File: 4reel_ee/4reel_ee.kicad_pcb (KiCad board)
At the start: 4 copper layers, 117.5 x 30 mm, 152 parts, among them J1 USB_C_Receptacle_USB2.0_16P, J2 Micro_SD_Card_Det2, J3 RJ45_Hanrun_HR911105A_Horizon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, J4 JST, U1 RV1103G, U2 EA3036C, U3 ImageSensor_OV9281, U4 TLV73312PDBV, U5 TPD2EUSB30, U6 TLV73328PDBV, U7 W25Q32JVZP, U8 LIS2HH12, U9 ImageSensor_OV9281, Y1 TXC-7C, Y2 24Mhz, Y3 TXC-7C

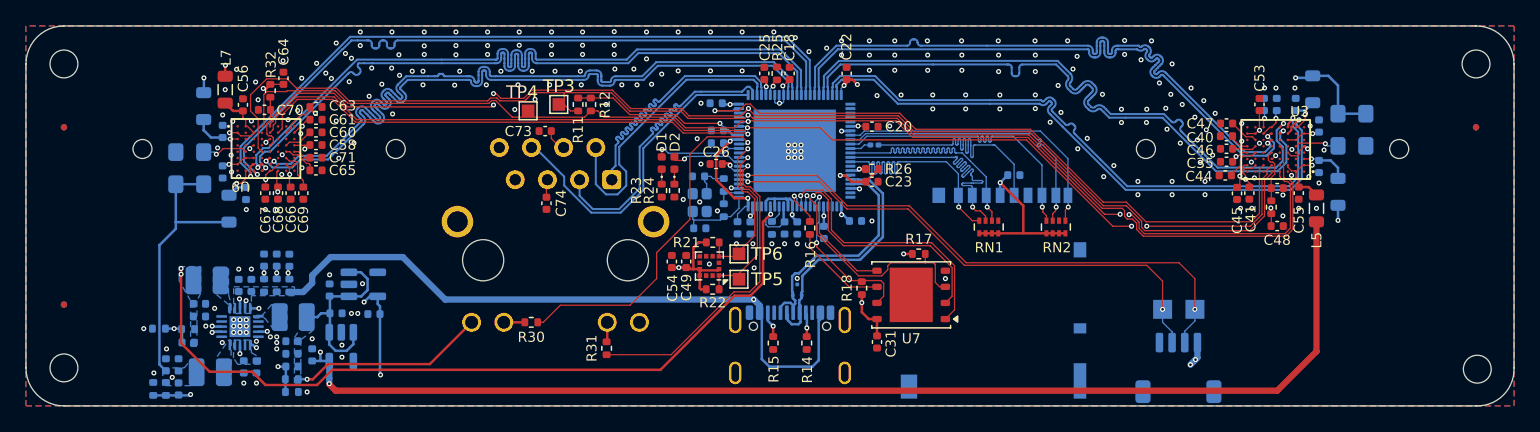
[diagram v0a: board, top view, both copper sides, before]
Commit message: Initial schematic, routing finished for RV1106 based design.
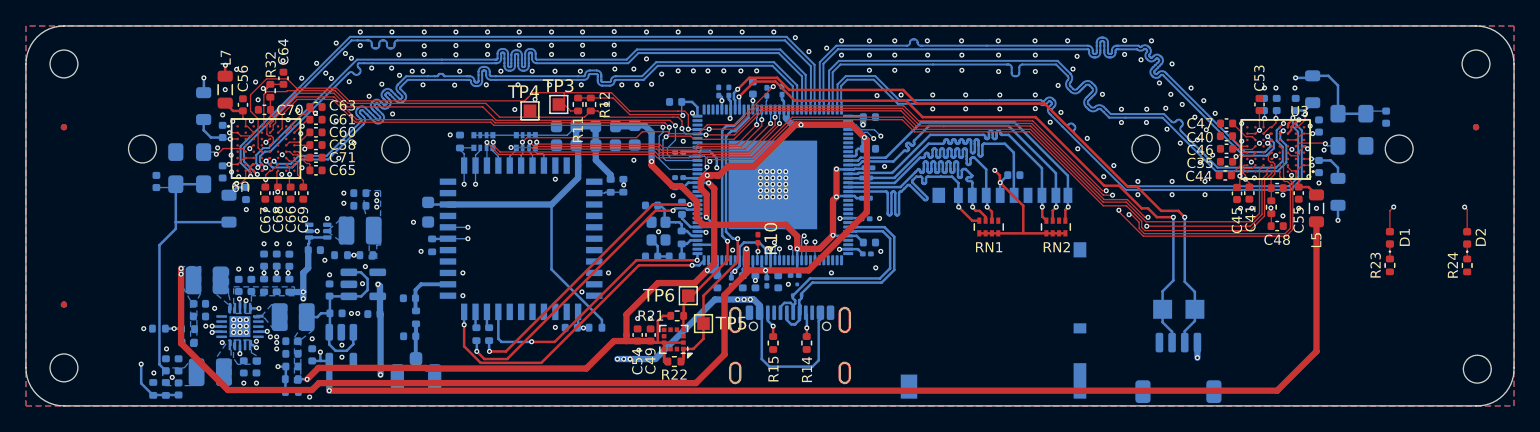
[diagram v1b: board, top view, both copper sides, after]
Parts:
- removed R18, R26: 10k, Resistor_SMD:R_0402_1005Metric
- added C76: 100nF, Capacitor_SMD:C_0201_0603Metric, B.Cu at (123.7, 105.2)
- added C77: 10uF, Capacitor_SMD:C_0402_1005Metric, B.Cu at (127.4, 105.2)
- added C78: 100nF, Capacitor_SMD:C_0201_0603Metric, B.Cu at (134.3, 100.2)
- added C79: 10uF, Capacitor_SMD:C_0402_1005Metric, B.Cu at (94.4, 99.2)
- added C80: 100nF, Capacitor_SMD:C_0201_0603Metric, B.Cu at (134.3, 98.6)
- added C81: 10uF, Capacitor_SMD:C_0603_1608Metric, B.Cu at (110.7, 94.4)
- added C82: NC, Capacitor_SMD:C_0402_1005Metric, B.Cu at (111.1, 108.8)
- added C83: 10uF, Capacitor_SMD:C_0603_1608Metric, B.Cu at (110.7, 92.9)
- added C84: 10uF, Capacitor_SMD:C_0603_1608Metric, B.Cu at (116.1, 93.6)
- added C85: 10uF, Capacitor_SMD:C_0603_1608Metric, B.Cu at (113.8, 94.4)
- added C86: 100nF, Capacitor_SMD:C_0201_0603Metric, B.Cu at (119.6, 95.0)
- added C87: 100nF, Capacitor_SMD:C_0201_0603Metric, B.Cu at (119.6, 97.0)
- added C88: 100nF, Capacitor_SMD:C_0201_0603Metric, B.Cu at (119.6, 97.8)
- added C89: 100nF, Capacitor_SMD:C_0201_0603Metric, B.Cu at (123.5, 90.2)
- added C90: 100nF, Capacitor_SMD:C_0201_0603Metric, B.Cu at (134.5, 96.2)
- added C91: 100nF, Capacitor_SMD:C_0201_0603Metric, B.Cu at (122.7, 90.2)
- added C92: 10uF, Capacitor_SMD:C_0603_1608Metric, B.Cu at (99.8, 99.7)
- added C93: 10uF, Capacitor_SMD:C_0402_1005Metric, B.Cu at (94.4, 98.2)
- added L10: 120R@100MHz, Inductor_SMD:L_0603_1608Metric, B.Cu at (113.8, 92.9)
- added L11: 1uH, Inductor_SMD:L_1008_2520Metric, B.Cu at (94.4, 101.2)
- added R28: 22R, Resistor_SMD:R_0201_0603Metric, B.Cu at (126.5, 90.2)
- added R29: 1k, Resistor_SMD:R_0402_1005Metric, B.Cu at (104.6, 109.3)
- added R33: 1k, Resistor_SMD:R_0402_1005Metric, B.Cu at (103.6, 109.3)
- added R34: 100k, Resistor_SMD:R_0402_1005Metric, B.Cu at (113.0, 108.8)
- added R35: 10k, Resistor_SMD:R_0402_1005Metric, B.Cu at (114.2, 97.6)
- added R36: 0R, Resistor_SMD:R_0402_1005Metric, B.Cu at (115.2, 97.6)
- added RN3: 10k, Resistor_SMD:R_Array_Convex_4x0402, B.Cu at (104.1, 94.1)
- added RN4: 10k, Resistor_SMD:R_Array_Convex_4x0402, B.Cu at (107.5, 94.1)
- added U10: RTL8723DS, KiLib:RTL8723, B.Cu at (107.1, 101.8)
- C18: footprint Capacitor_SMD:C_0402_1005Metric -> Capacitor_SMD:C_0201_0603Metric; moved to B.Cu
- C20, C22, C23, C25, C26: moved to B.Cu
- C24, C28, C75: footprint Capacitor_SMD:C_0402_1005Metric -> Capacitor_SMD:C_0201_0603Metric
- C31: value 100nF -> 10uF; moved to B.Cu
- C73, C74: value 10nF -> NC; moved to B.Cu
- J3: value RJ45_Hanrun_HR911105A_Horizontal -> Conn_Coaxial; footprint Connector_RJ:RJ45_Hanrun_HR911105A_Horizontal -> Connector_Coaxial:U.FL_Hirose_U.FL-R-SMT-1_Vertical
- R10: footprint Resistor_SMD:R_0402_1005Metric -> Resistor_SMD:R_0201_0603Metric; moved to F.Cu
- R16: value 22R -> 100k; moved to B.Cu
- R17: value 10k -> 80k; moved to B.Cu
- R25: value 6.04k -> 10K; moved to B.Cu
- R30: value 330R -> 0R; moved to B.Cu
- R31: value 330R -> 100K; moved to B.Cu
- U1: value RV1103G -> RV1106G3; footprint rv1103b:Rockchip_QFN-88-1EP_9x9mm_P0.35mm_EP6.5x6.5mm -> rv1106:Rockchip_QFN-128-1EP_12.3x12.3mm_P0.35mm_EP7x7mm
- U7: value W25Q32JVZP -> TPS62A01ADRL; footprint Package_SON:WSON-8-1EP_6x5mm_P1.27mm_EP3.4x4.3mm -> Package_TO_SOT_SMD:SOT-563; moved to B.Cu
- moved D2 62.9 mm to (181.8, 101.7)
- moved R24 62.9 mm to (181.8, 103.9)
- moved D1 57.8 mm to (175.7, 101.7)
- moved R23 57.8 mm to (175.7, 103.9)
- moved C37 52.8 mm to (175.4, 92.2), turned to -90 degrees
- moved U7 47.1 mm to (91.1, 101.2)
- moved R17 45.6 mm to (92.9, 103.1), turned to 180 degrees
- moved C31 45.0 mm to (90.8, 102.7), turned to 0 degrees
- moved C72 44.6 mm to (78.3, 97.3), turned to 90 degrees
- moved R16 35.1 mm to (94.9, 103.1), turned to 180 degrees
- moved R25 25.6 mm to (102.3, 94.1)
- moved J3 22.0 mm to (98.8, 112.8), turned to -90 degrees
- moved C73 19.4 mm to (98.3, 109.5)
- moved R31 16.0 mm to (100.1, 102.3)
- moved C22 13.7 mm to (119.3, 91.0), turned to 180 degrees
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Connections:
- net /MPU/SDMMC.CLK renamed /MPU/SDMMC1.CLK
- C31 pad 1: +3V3 -> +5V
- C32 pad 1: Net-(U1GPIO / Peripherals-OSC_SOC_XIN) -> Net-(U1Analog / Connectivity-OSC_XOUT)
- C73 pad 1: Net-(J3-TCT) -> Net-(J3-In)
- C74 pad 1: Net-(J3-RCT) -> Net-(U10-WIFI/BT_ANT)
- J2 pad 1: /MPU/SDMMC.D2 -> /MPU/SDMMC1.D2
- J2 pad 2: /MPU/SDMMC.D3 -> /MPU/SDMMC1.D3
- J2 pad 3: /MPU/SDMMC.CMD -> /MPU/SDMMC1.CMD
- J2 pad 7: /MPU/SDMMC.D0 -> /MPU/SDMMC1.D0
- J2 pad 8: /MPU/SDMMC.D1 -> /MPU/SDMMC1.D1
- J2 pad 9: /MPU/SDMMC.DET -> /MPU/SDMMC1.DET
- J3 pad 1: /MPU/EPHY.TXP -> Net-(J3-In)
- J3 pad 2: /MPU/EPHY.TXN -> GND
- R10 pad 2: Net-(U1Analog / High-Speed-DRAM_ZQ) -> Net-(U1Analog / Connectivity-DRAM_ZQ)
- R16 pad 1: Net-(U1Analog / High-Speed-FSPI_CLK) -> +1V35
- R16 pad 2: /Flash/FSPI.CLK -> Net-(U7-FB)
- R17 pad 1: +3V3 -> Net-(U7-FB)
- R17 pad 2: /Flash/FSPI.D2 -> GND
- R19 pad 2: Net-(U1GPIO / Peripherals-OSC_SOC_XOUT) -> Net-(U1Analog / Connectivity-OSC_XIN)
- R20 pad 1: Net-(U1GPIO / Peripherals-OSC_SOC_XOUT) -> Net-(U1Analog / Connectivity-OSC_XIN)
- R20 pad 2: Net-(U1GPIO / Peripherals-OSC_SOC_XIN) -> Net-(U1Analog / Connectivity-OSC_XOUT)
- R25 pad 2: Net-(U1Analog / High-Speed-FEPHY_EXTR) -> /MPU/WL_REG_ON
- R27 pad 1: Net-(U1GPIO / Peripherals-SDMMC_CLK) -> Net-(U1Storage-SDMMC0_CLK)
- R30 pad 1: /LED_ACT -> Net-(J3-In)
- R30 pad 2: Net-(J3-Pad11) -> Net-(U10-WIFI/BT_ANT)
- R31 pad 1: /LED100 -> GND
- R31 pad 2: Net-(J3-Pad10) -> /MPU/BT_WAKE
- RN1 pad 2: /MPU/SDMMC.CMD -> /MPU/SDMMC1.CMD
- RN1 pad 3: /MPU/SDMMC.D3 -> /MPU/SDMMC1.D3
- RN1 pad 4: /MPU/SDMMC.D2 -> /MPU/SDMMC1.D2
- RN2 pad 1: /MPU/SDMMC.DET -> /MPU/SDMMC1.DET
- RN2 pad 3: /MPU/SDMMC.D1 -> /MPU/SDMMC1.D1
- RN2 pad 4: /MPU/SDMMC.D0 -> /MPU/SDMMC1.D0
- U1 pad 1: unconnected-(U1Analog / High-Speed-MIPI_CLK0_OUT-Pad1) -> +1V8
- U1 pad 10: /MPU/SDMMC.D0 -> +0V9
- U1 pad 11: Net-(U1GPIO / Peripherals-SDMMC_CLK) -> /MPU/SDMMC1.DET
- U1 pad 12: /MPU/SDMMC.CMD -> /MPU/SDMMC1.D1
- U1 pad 13: /MPU/SDMMC.D3 -> +3V3
- U1 pad 14: /MPU/SDMMC.D2 -> /MPU/SDMMC1.D0
- U1 pad 15: unconnected-(U1Analog / High-Speed-SARADC_IN1-Pad15) -> Net-(U1Storage-SDMMC0_CLK)
- U1 pad 16: Net-(U1Analog / High-Speed-SARADC_IN0) -> /MPU/SDMMC1.CMD
- U1 pad 17: +1V8 -> /MPU/SDMMC1.D3
- U1 pad 18: /MPU/USB.DN -> /MPU/SDMMC1.D2
- U1 pad 19: /MPU/USB.DP -> +3V3
- U1 pad 20: +3V3 -> unconnected-(U1Analog / Connectivity-RTC_XOUT-Pad20)
- U1 pad 23: +1V8 -> unconnected-(U1Analog / Connectivity-SARADC_IN0-Pad23)
- U1 pad 24: unconnected-(U1GPIO / Peripherals-CODEC_MIC0P_MICP-Pad24) -> +1V8
- U1 pad 26: unconnected-(U1GPIO / Peripherals-CODEC_MIC1P_MICN-Pad26) -> /MPU/USB.DN
- U1 pad 27: +3V3 -> /MPU/USB.DP
- U1 pad 28: /Flash/FSPI.D3 -> +3V3
- U1 pad 29: /Flash/FSPI.D0 -> unconnected-(U1Analog / Connectivity-CODEC_LINEOUT-Pad29)
- U1 pad 3: unconnected-(U1GPIO / Peripherals-PWM7_IR_M2-Pad3) -> /MPU/LED2
- U1 pad 30: /Flash/FSPI.D1 -> unconnected-(U1Analog / Connectivity-CODEC_VCM-Pad30)
- U1 pad 31: /Flash/FSPI.D2 -> +1V8
- U1 pad 32: /Flash/FSPI.~{CS} -> unconnected-(U1Analog / Connectivity-CODEC_MICBIAS-Pad32)
- U1 pad 33: Net-(U1Analog / High-Speed-FSPI_CLK) -> unconnected-(U1Analog / Connectivity-CODEC_MIC0N-Pad33)
- U1 pad 34: +1V8 -> unconnected-(U1Analog / Connectivity-CODEC_MIC0P-Pad34)
- U1 pad 35: +1V8 -> unconnected-(U1Analog / Connectivity-CODEC_MIC1N-Pad35)
- U1 pad 36: +0V9 -> unconnected-(U1Analog / Connectivity-CODEC_MIC1P-Pad36)
- U1 pad 37: Net-(U1Analog / High-Speed-DRAM_ZQ) -> GND
- U1 pad 38: +1V8 -> unconnected-(U1Storage-EMMC_D5-Pad38)
- U1 pad 39: +0V9 -> /MPU/BT_LPO
- U1 pad 4: unconnected-(U1GPIO / Peripherals-I2C4_SCL_M2-Pad4) -> /MPU/LED1
- U1 pad 40: +1V8 -> unconnected-(U1Storage-EMMC_D4-Pad40)
- U1 pad 41: GND -> /MPU/WL_HOST_WAKE
- U1 pad 42: unconnected-(U1Analog / High-Speed-PWR_CTRL_M0-Pad42) -> /MPU/WL_REG_ON
- U1 pad 44: +0V9 -> /MPU/BT_HOST_WAKE
- U1 pad 45: Net-(U1GPIO / Peripherals-OSC_SOC_XIN) -> unconnected-(U1Storage-EMMC_D6-Pad45)
- U1 pad 46: Net-(U1GPIO / Peripherals-OSC_SOC_XOUT) -> unconnected-(U1Storage-EMMC_D7-Pad46)
- U1 pad 47: +1V8 -> /MPU/BT_WAKE
- U1 pad 48: unconnected-(U1GPIO / Peripherals-PWM0_M0-Pad48) -> /MPU/~{BT_RST}
- U1 pad 49: /MPU/UART_RX -> +1V35
- U1 pad 50: /MPU/UART_TX -> +1V35
- U1 pad 51: +3V3 -> +0V9
- U1 pad 52: /LED100 -> Net-(U1Analog / Connectivity-DRAM_ZQ)
- U1 pad 53: /MPU/LED2 -> +1V8
- U1 pad 54: /Accelerometer/I2C3.SCL -> +0V9
- U1 pad 55: /Accelerometer/I2C3.SDA -> +0V9
- U1 pad 56: /MPU/LED1 -> +1V35
- U1 pad 57: /LED_ACT -> GND
- U1 pad 58: +0V9 -> unconnected-(U1GPIO / Peripherals-UART0_RX_M0-Pad58)
- U1 pad 59: +1V8 -> unconnected-(U1GPIO / Peripherals-UART0_TX_M0-Pad59)
- U1 pad 6: +0V9 -> unconnected-(U1Camera / Display-VI_CIF_D13-Pad6)
- U1 pad 60: /MPU/STROBE2 -> unconnected-(U1GPIO / Peripherals-PWM3_IR_M0-Pad60)
- U1 pad 61: /MPU/VSYNC -> +3V3
- U1 pad 62: /MPU/I2C4.SDA -> unconnected-(U1GPIO / Peripherals-PMIC_PWR_CTRL_M1-Pad62)
- U1 pad 63: /MPU/I2C4.SCL -> unconnected-(U1GPIO / Peripherals-PMIC_PWR_CTRL_M0-Pad63)
- U1 pad 64: /MPU/XSHUTDOWN -> /MPU/UART1.~{RTS}
- U1 pad 65: /MPU/STROBE1 -> /MPU/UART1.~{CTS}
- U1 pad 66: +1V8 -> unconnected-(U1Power / System-nPOR-Pad66)
- U1 pad 67: /MPU/EPHY.RXN -> +0V9
- U1 pad 68: /MPU/EPHY.RXP -> Net-(U1Analog / Connectivity-OSC_XIN)
- U1 pad 69: /MPU/EPHY.TXN -> Net-(U1Analog / Connectivity-OSC_XOUT)
- U1 pad 7: +3V3 -> unconnected-(U1Camera / Display-VI_CIF_D12-Pad7)
- U1 pad 70: /MPU/EPHY.TXP -> +1V8
- U1 pad 71: +3V3 -> +0V9
- U1 pad 72: Net-(U1Analog / High-Speed-FEPHY_EXTR) -> unconnected-(U1GPIO / Peripherals-UART3_TX_M0-Pad72)
- U1 pad 73: +0V9 -> unconnected-(U1GPIO / Peripherals-UART3_RX_M0-Pad73)
- U1 pad 74: +0V9 -> unconnected-(U1GPIO / Peripherals-PWM0_M0-Pad74)
- U1 pad 75: +0V9 -> /MPU/UART1.TXD
- U1 pad 76: /MPU/MIPI2.D1N -> /MPU/UART1.RXD
- U1 pad 77: /MPU/MIPI2.D1P -> unconnected-(U1GPIO / Peripherals-UART4_RX_M0-Pad77)
- U1 pad 78: /MPU/MIPI2.CK0N -> unconnected-(U1GPIO / Peripherals-UART4_TX_M0-Pad78)
- U1 pad 79: /MPU/MIPI2.CK0P -> unconnected-(U1GPIO / Peripherals-JTAG_CPU_TCK_M1-Pad79)
- U1 pad 8: /MPU/SDMMC.DET -> unconnected-(U1Camera / Display-VI_CIF_D14-Pad8)
- U1 pad 80: /MPU/MIPI2.D0N -> unconnected-(U1GPIO / Peripherals-JTAG_CPU_TMS_M1-Pad80)
- U1 pad 81: /MPU/MIPI2.D0P -> +3V3
- U1 pad 82: /MPU/MIPI1.D1N -> +0V9
- U1 pad 83: /MPU/MIPI1.D1P -> /MPU/STROBE1
- U1 pad 84: /MPU/MIPI1.CK0N -> /MPU/STROBE2
- U1 pad 85: /MPU/MIPI1.CK0P -> unconnected-(U1Camera / Display-VO_LCDC_CLK-Pad85)
- U1 pad 86: /MPU/MIPI1.D0N -> /MPU/VSYNC
- U1 pad 87: /MPU/MIPI1.D0P -> /MPU/XSHUTDOWN
- U1 pad 89: GND -> unconnected-(U1Camera / Display-VO_LCDC_DEN-Pad89)
- U1 pad 9: /MPU/SDMMC.D1 -> unconnected-(U1Camera / Display-VI_CIF_D15-Pad9)
- U7 pad 1: /Flash/FSPI.~{CS} -> GND
- U7 pad 2: /Flash/FSPI.D1 -> Net-(U7-SW)
- U7 pad 3: /Flash/FSPI.D2 -> +5V
- U7 pad 4: GND -> +5V
- U7 pad 5: /Flash/FSPI.D0 -> Net-(U7-FB)
- U7 pad 6: /Flash/FSPI.CLK -> unconnected-(U7-PG-Pad6)
- Y2 pad 1: Net-(U1GPIO / Peripherals-OSC_SOC_XIN) -> Net-(U1Analog / Connectivity-OSC_XOUT)
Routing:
- net /MPU/LED2: track 5.41 -> 62.3 mm, vias 1 -> 2
- net /MPU/LED1: track 6.95 -> 62.6 mm, vias 1 -> 2
- net +1V35: track 0.00 -> 52.9 mm, vias 0 -> 5
- net +3.3VA: track 0.00 -> 43.4 mm
- net /MPU/WL_REG_ON: track 0.00 -> 35.6 mm, vias 0 -> 2
- net /MPU/WL_HOST_WAKE: track 0.00 -> 34.1 mm, vias 0 -> 2
- net /MPU/BT_WAKE: track 0.00 -> 30.0 mm, vias 0 -> 2
- net /MPU/BT_HOST_WAKE: track 0.00 -> 29.7 mm, vias 0 -> 2
- net /LED_ACT: track 27.8 -> 0.00 mm, vias 1 -> 0
- net /MPU/SDMMC2.D2: track 0.00 -> 27.7 mm, vias 0 -> 2
- net /MPU/SDMMC2.D3: track 0.00 -> 27.1 mm, vias 0 -> 2
- net +0V9: track 98.9 -> 126.0 mm, vias 8 -> 9
- net /MPU/UART1.~{RTS}: track 0.00 -> 25.6 mm, vias 0 -> 2
- net /MPU/EPHY.RXN: track 25.4 -> 0.00 mm
- net /MPU/EPHY.RXP: track 25.3 -> 0.00 mm
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- added copper zone on B.Cu, net +1V35
- added copper zone on B.Cu, net Net-(U7-SW)
